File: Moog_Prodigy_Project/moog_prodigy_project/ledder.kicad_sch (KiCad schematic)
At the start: 37 parts, among them J100 NJ2FD-V, Q100 CA3046, Q101 CA3046, Q102 BC327, Q103 BC556, U100 LT1469, U101 LT1228, U102 NE5532

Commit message: PCB priprema i fix gresaka
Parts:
- RV101: footprint Resistor_THT:R_Axial_DIN0207_L6.3mm_D2.5mm_P7.62mm_Horizontal -> Potentiometer_THT:Potentiometer_Bourns_3339P_Vertical_HandSoldering
- RV102: footprint Potentiometer_THT:Potentiometer_ACP_CA9-V10_Vertical -> Potentiometer_THT:Potentiometer_Bourns_3339P_Vertical_HandSoldering
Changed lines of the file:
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@@
 			)
 		)
-		(property "Footprint" "Potentiometer_THT:Potentiometer_ACP_CA9-V10_Vertical"
+		(property "Footprint" "Potentiometer_THT:Potentiometer_Bourns_3339P_Vertical_HandSoldering"
 			(at 109.22 93.98 0)
 			(effects
@@
 			)
 		)
-		(property "Footprint" "Resistor_THT:R_Axial_DIN0207_L6.3mm_D2.5mm_P7.62mm_Horizontal"
+		(property "Footprint" "Potentiometer_THT:Potentiometer_Bourns_3339P_Vertical_HandSoldering"
 			(at 85.09 93.98 0)
 			(effects

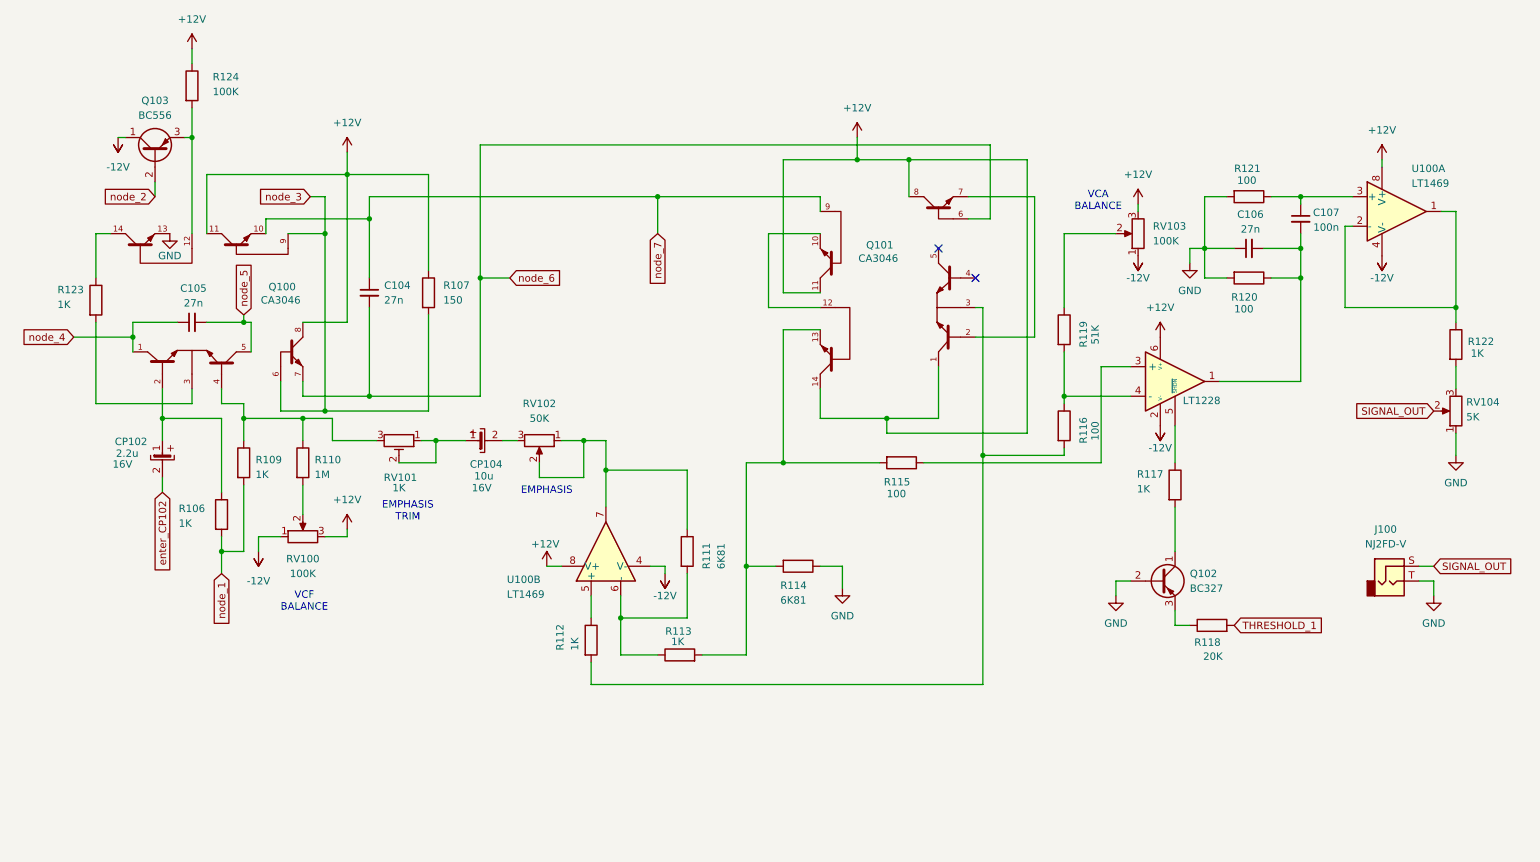
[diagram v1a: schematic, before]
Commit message: problemi sa ca3096, multiplicirani footprintovi
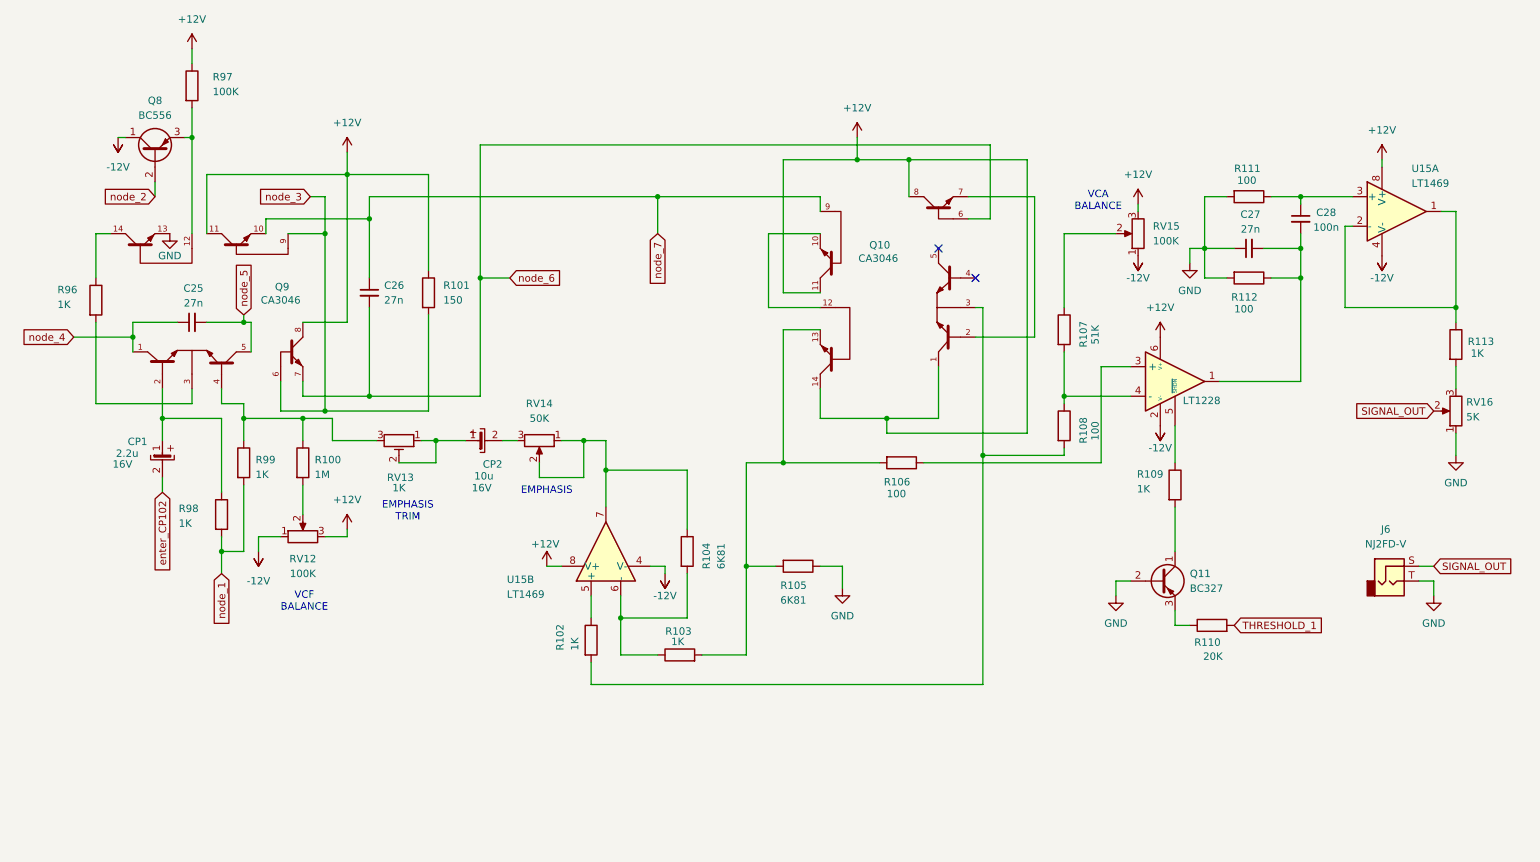
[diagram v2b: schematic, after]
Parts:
- renumbered C105 to C25, C104 to C26, C106 to C27, C107 to C28, CP102 to CP1, CP104 to CP2, J100 to J6, Q101 to Q10, Q102 to Q11, Q103 to Q8, Q100 to Q9, R110 to R100, R107 to R101, R112 to R102, R113 to R103, R111 to R104, R114 to R105, R115 to R106, R119 to R107, R116 to R108, R117 to R109, R118 to R110, R121 to R111, R120 to R112, R122 to R113, R123 to R96, R124 to R97, R106 to R98, R109 to R99, RV100 to RV12, RV101 to RV13, RV102 to RV14, RV103 to RV15, RV104 to RV16, U100 to U15, U101 to U16, U102 to U17

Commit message: Fix 1 nakon review-a 27.05.2026
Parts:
- removed unit 3 of U15
- removed unit 2 of U15
- added U1: LT1469, Package_DIP:DIP-8_W7.62mm, symbol Amplifier_Operational:NE5532
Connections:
- net +12V: now also Q10., Q9., U1.8 (V+); no longer Q10.1, Q10.11, Q10.14, Q10.8, Q9.11, Q9.8
- net -12V: now also Q8. (E), U1.4 (V-); no longer Q8.1 (C)
- net GND: now also Q11. (E), Q9.; no longer Q11.2 (B), Q9.13
- net node_2: now also Q8. (E); no longer Q8.2 (B)
- net node_3: now also Q9.; no longer Q9.6, Q9.9
- net node_4: now also Q9.; no longer Q9.1
- net node_6: now also Q10., Q9.; no longer Q10.6, Q9.7
- net node_7: now also Q10., Q9.; no longer Q10.9, Q9.10
- net at R102.1: now also U1.5 (+)
- net at R102.2, R108.2: now also Q10.; no longer Q10.3
- net at R110.1: now also Q11. (E); no longer Q11.3 (E)
- net at R109.2: now also Q11. (E); no longer Q11.1 (C)
- net at R96.1: now also Q9.; no longer Q9.14
- net at CP1.1, R98.1: now also Q9.; no longer Q9.2
- net at R96.2: now also Q9.; no longer Q9.3
- net at R100.1, R99.1, RV13.3: now also Q9.; no longer Q9.4
- net at R103.1, R104.2: now also U1.6 (-)
- net at R103.2, R105.2, R106.2: now also Q10.; no longer Q10.13
- net at R104.1, RV14.1, RV14.2: now also U1.7
- new net: Q8. (E), Q9., R97.2
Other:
- moved on the sheet: R102, R104

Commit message: Latest checkpoints update 05.06.2026
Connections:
- net enter_CP102: now also CP1.; no longer CP1.2
- net at RV14.3: now also CP2.; no longer CP2.2
- net at RV13.1, RV13.2: now also CP2.; no longer CP2.1
- new net: Q8. (E), Q9., R97.2
- new net: CP1., Q9., R98.1
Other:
- moved on the sheet: Q11, R110, R113, RV16

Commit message: 27.06.2026 - dodavanje izmena sa konsultacija
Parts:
- added C71, C72, C73, C74, C75, C76: 100n, Capacitor_THT:CP_Radial_D5.0mm_P2.50mm, symbol Device:C
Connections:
- net +12V: now also C71.2, C74.2, C75.2
- net -12V: now also C72.2, C73.2, C76.2
- net GND: now also C71.1, C72.1, C73.1, C74.1, C75.1, C76.1
- new net: Q8. (E), Q9., R97.2
- new net: CP1., Q9., R98.1
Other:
- note added: "NAPOMENA Kondenzatori: C71,C72,C73,C74,C75,C76 su vrednosti 100n i oni su kvalitetniji"
- moved on the sheet: R103, R104
